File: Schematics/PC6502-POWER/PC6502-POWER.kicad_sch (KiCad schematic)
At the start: 52 parts, among them J1 BUS, J2 694106301002, J5 USB_C_Receptacle_USB2.0_16P, J6 ST4500 PROG, K1 G6RL-1_DC24, K2 G6RL-1_DC24, Q1 STL9P3LLH6, U1 UWS-5/10-Q12P-C, U2 STUSB4500QTR, U3 0031.8211

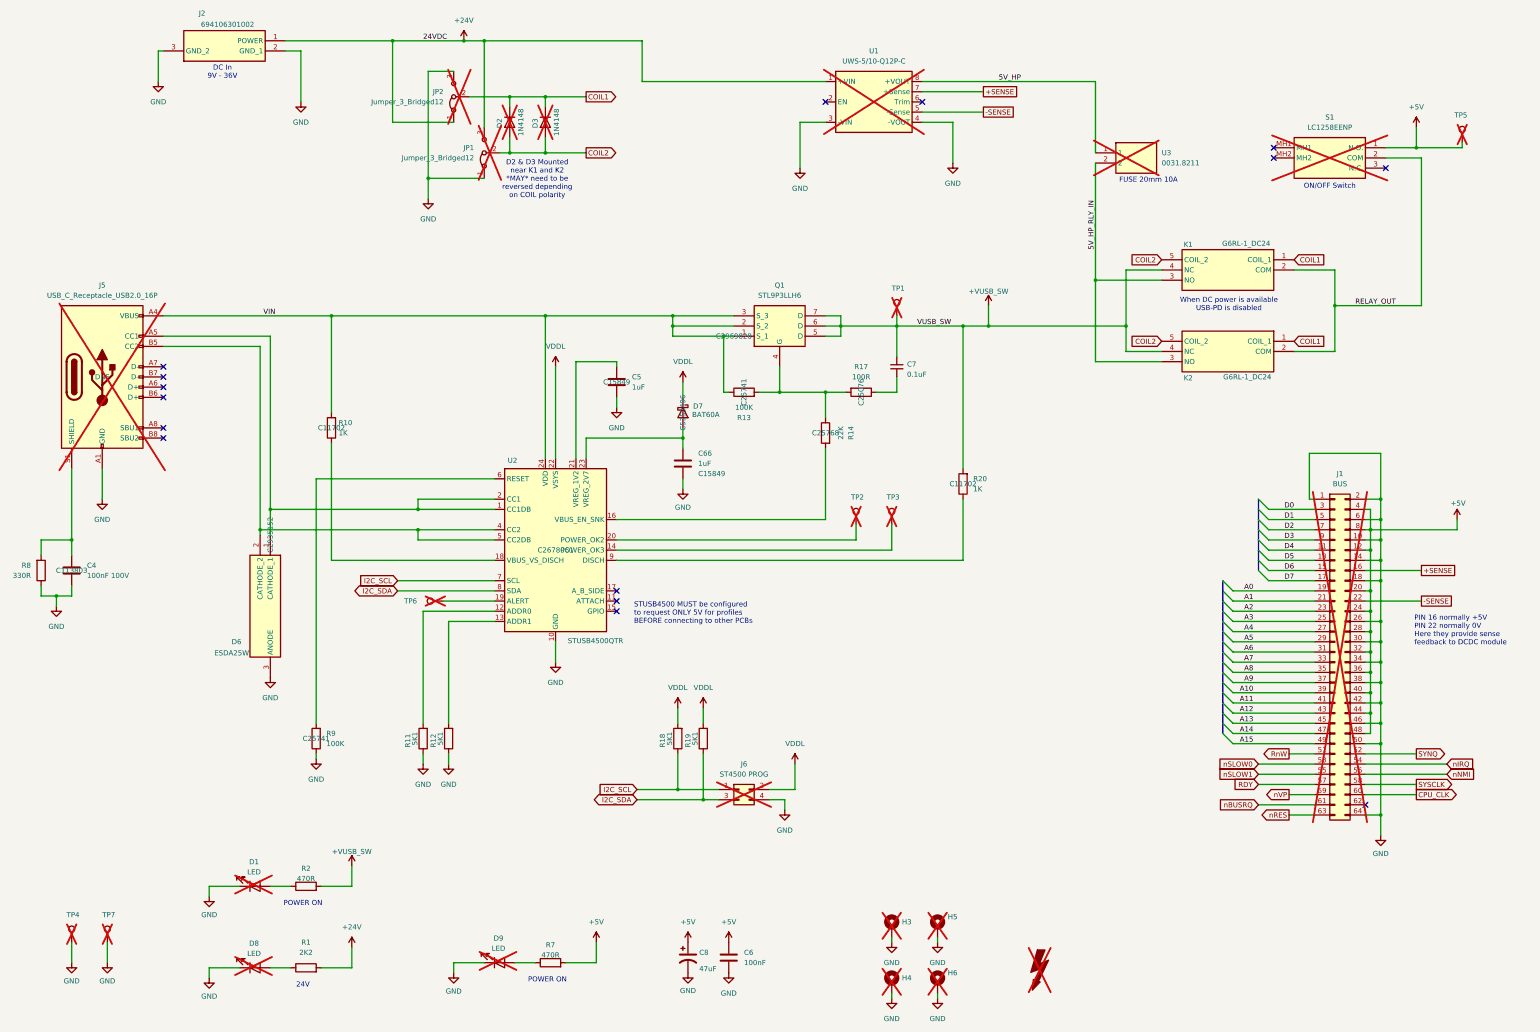
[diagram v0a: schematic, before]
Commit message: Tidy up and simplify
Created schematic for FM & Speech sound board
Made Storage board just for Compact Flash (CF) storage
Routed Storage PCB
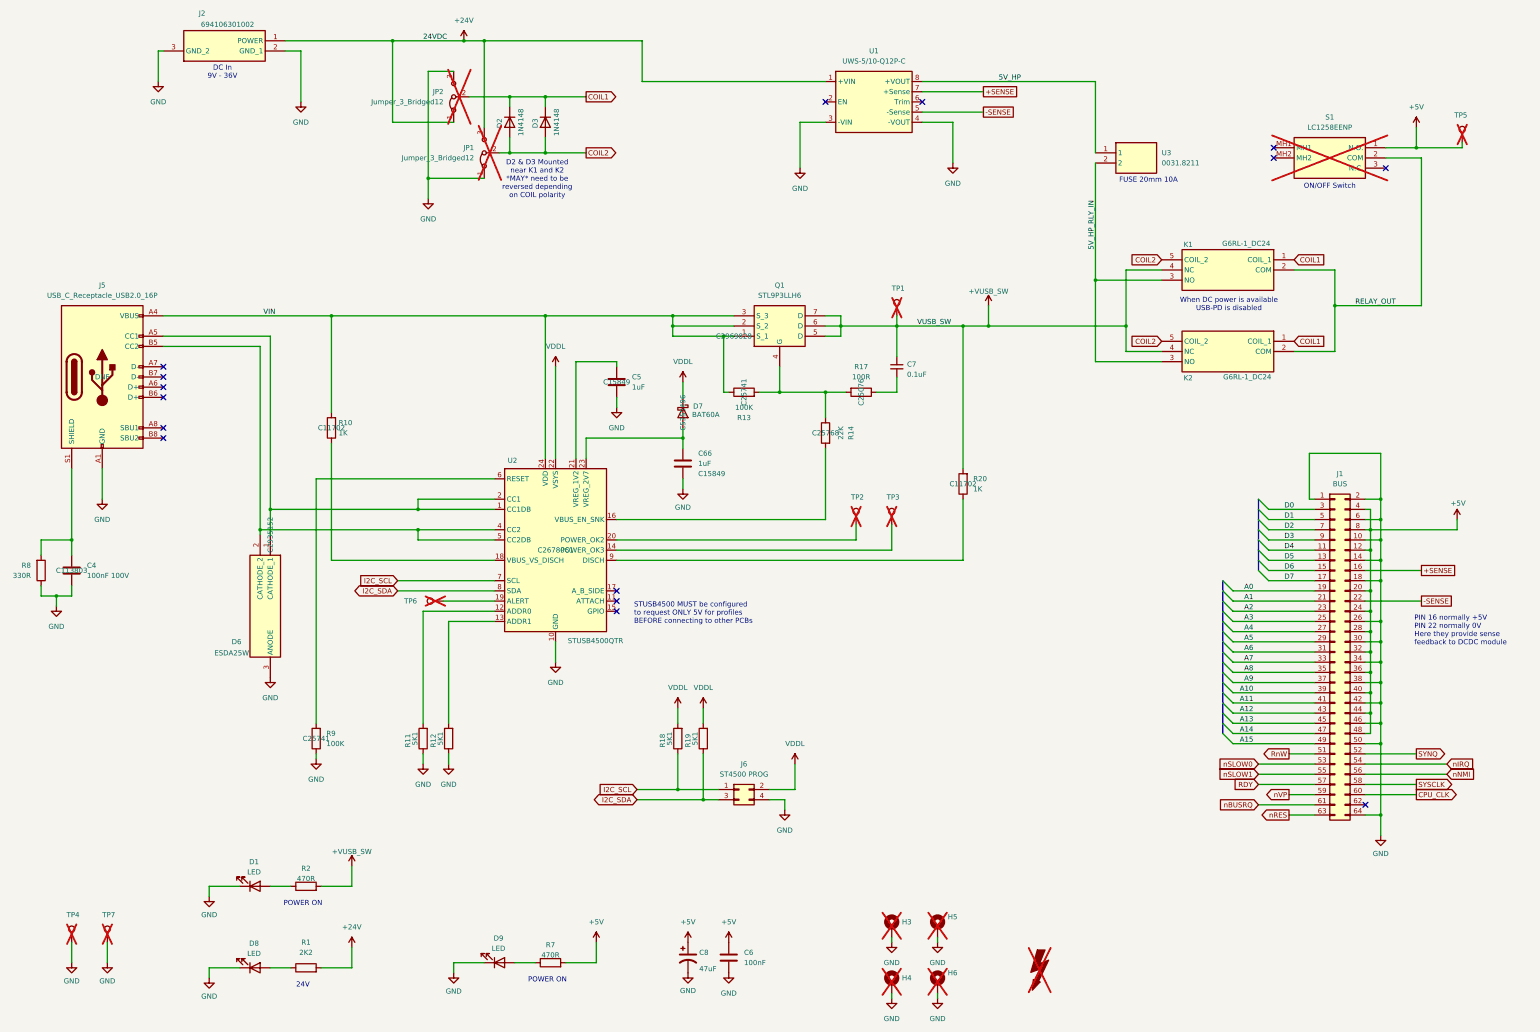
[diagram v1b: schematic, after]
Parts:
- D1, D2, D3, D8, D9, J1, J5, J6, U1, U3: now fitted
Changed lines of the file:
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@@
 		(in_bom yes)
 		(on_board yes)
-		(dnp yes)
+		(dnp no)
 		(property "Reference" "D3"
 			(at 154.94 49.784 0)
@@
 		(in_bom yes)
 		(on_board yes)
-		(dnp yes)
+		(dnp no)
 		(property "Reference" "D1"
 			(at 84.836 233.934 0)
@@
 		(in_bom yes)
 		(on_board yes)
-		(dnp yes)
+		(dnp no)
 		(property "Reference" "D8"
 			(at 84.836 254.254 0)
@@
 		(in_bom yes)
 		(on_board yes)
-		(dnp yes)
+		(dnp no)
 		(property "Reference" "D2"
 			(at 146.05 49.784 0)
@@
 		(in_bom yes)
 		(on_board yes)
-		(dnp yes)
+		(dnp no)
 		(property "Reference" "D9"
 			(at 145.796 252.984 0)
@@
 		(in_bom yes)
 		(on_board yes)
-		(dnp yes)
+		(dnp no)
 		(fields_autoplaced yes)
 		(property "Reference" "J6"
@@
 		(in_bom yes)
 		(on_board yes)
-		(dnp yes)
+		(dnp no)
 		(fields_autoplaced yes)
 		(property "Reference" "U3"
@@
 		(in_bom yes)
 		(on_board yes)
-		(dnp yes)
+		(dnp no)
 		(property "Reference" "J1"
 			(at 355.6 137.16 0)
@@
 		(in_bom yes)
 		(on_board yes)
-		(dnp yes)
+		(dnp no)
 		(fields_autoplaced yes)
 		(property "Reference" "J5"
@@
 		(in_bom yes)
 		(on_board yes)
-		(dnp yes)
+		(dnp no)
 		(fields_autoplaced yes)
 		(property "Reference" "U1"
